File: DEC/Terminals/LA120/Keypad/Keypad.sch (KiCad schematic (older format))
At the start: 23 parts, among them J1 Conn_01x16, SW1 ENTER, SW10 9, SW11 0, SW12 COMMA, SW13 MINUS, SW14 PF1, SW15 PF2, SW16 PF3, SW17 PF4, SW18 PERIOD, SW2 1, SW3 2, SW4 3, SW5 4, SW6 5, SW7 6, SW8 7, SW9 8

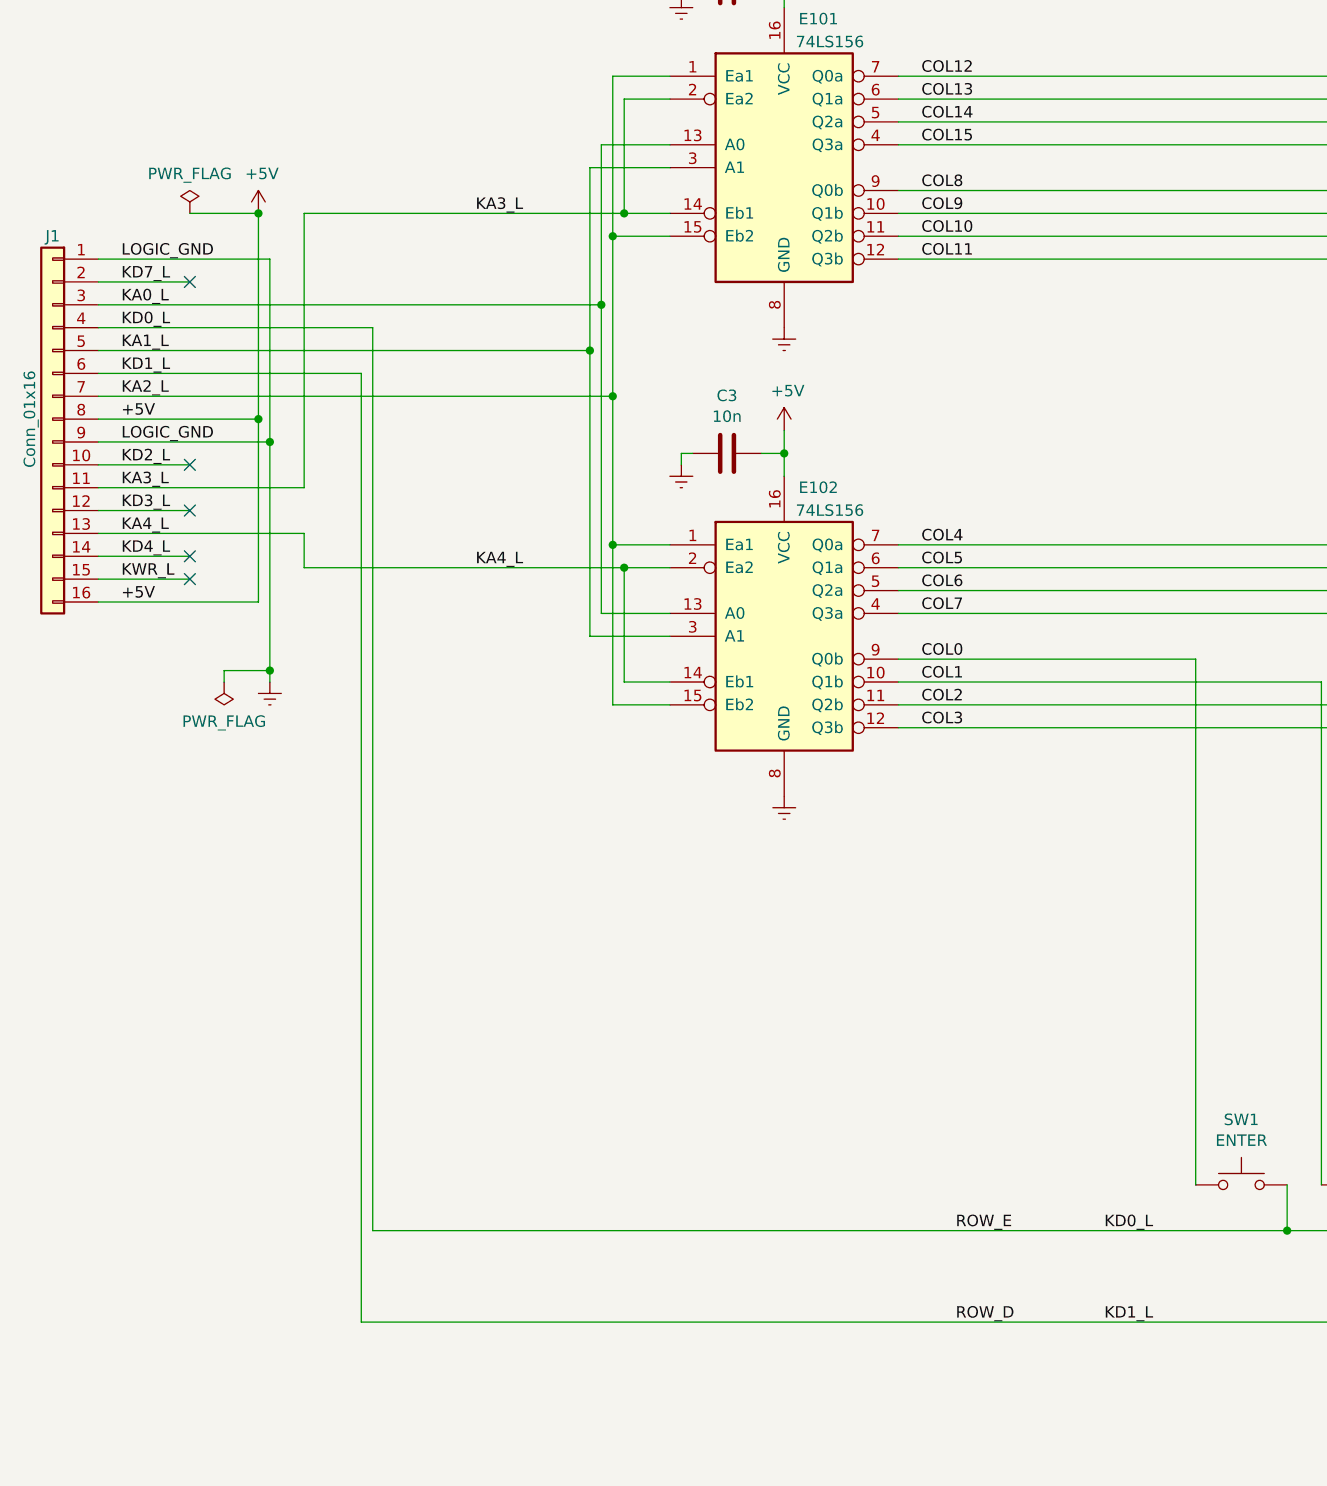
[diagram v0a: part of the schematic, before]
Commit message: Adds LA120 keyboard
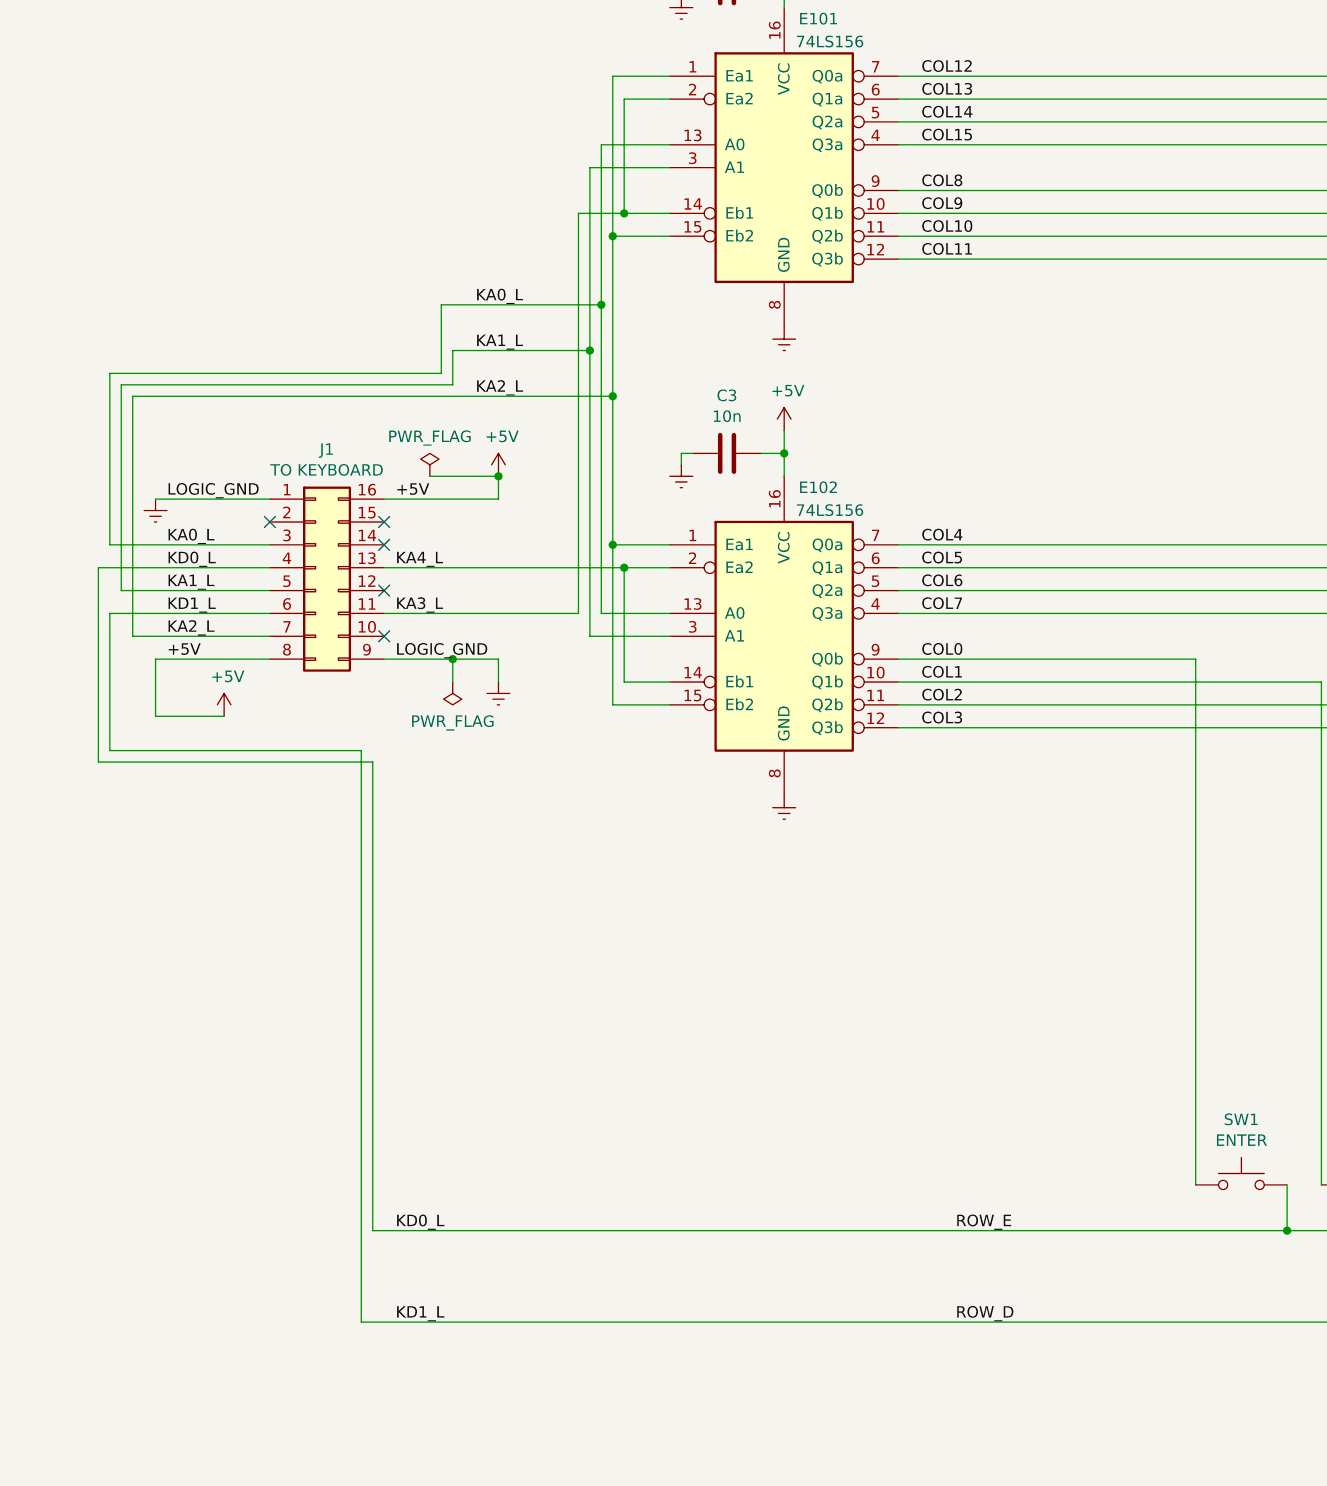
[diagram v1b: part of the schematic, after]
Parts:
- removed J1: Conn_01x16, symbol Connector_Generic:Conn_01x16
- added J1: TO KEYBOARD, symbol Connector_Generic:Conn_02x08_Counter_Clockwise
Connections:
- net +5V: now also J1.16 (Pin_16), J1.8 (Pin_8)
- net GNDREF: now also J1.1 (Pin_1), J1.9 (Pin_9)
- net KA0_L: now also J1.3 (Pin_3)
- net KA1_L: now also J1.5 (Pin_5)
- net KA2_L: now also J1.7 (Pin_7)
- net KA3_L: now also J1.11 (Pin_11)
- net KA4_L: now also J1.13 (Pin_13)
- net KD0_L: now also J1.4 (Pin_4)
- net KD1_L: now also J1.6 (Pin_6)
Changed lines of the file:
@@
 $EndDescr
-$Comp
-L Connector_Generic:Conn_01x16 J1
-U 1 1 5D1FAE3B
-P 1050 3750
-F 0 "J1" H 1050 4550 50  0000 C CNN
-F 1 "Conn_01x16" V 1150 3750 50  0000 C CNN
-F 2 "" H 1050 3750 50  0001 C CNN
-F 3 "~" H 1050 3750 50  0001 C CNN
-	1    1050 3750
-	-1   0    0    -1
-$EndComp
 $Comp
 L Switch:SW_Push SW1
@@
 	1    0    0    -1
 $EndComp
-Wire Wire Line
-	1250 3150 1650 3150
-Wire Wire Line
-	1250 3950 1650 3950
-Wire Wire Line
-	1250 4150 1650 4150
-Wire Wire Line
-	1250 4350 1650 4350
-Wire Wire Line
-	1250 4450 1650 4450
-Text Label 1350 3050 0    50   ~ 0
-LOGIC_GND
-Text Label 1350 3150 0    50   ~ 0
-KD7_L
-Text Label 1350 3750 0    50   ~ 0
-+5V
-Text Label 1350 4550 0    50   ~ 0
-+5V
-Text Label 1350 3850 0    50   ~ 0
-LOGIC_GND
-Text Label 1350 4050 0    50   ~ 0
-KA3_L
-Text Label 1350 4250 0    50   ~ 0
-KA4_L
-Text Label 1350 4450 0    50   ~ 0
-KWR_L
-Text Label 1350 3650 0    50   ~ 0
+Text Label 2900 3650 0    50   ~ 0
 KA2_L
-Text Label 1350 3450 0    50   ~ 0
+Text Label 2900 3450 0    50   ~ 0
 KA1_L
-Text Label 1350 3250 0    50   ~ 0
+Text Label 2900 3250 0    50   ~ 0
 KA0_L
-Text Label 1350 4350 0    50   ~ 0
-KD4_L
-Text Label 1350 4150 0    50   ~ 0
-KD3_L
-Text Label 1350 3950 0    50   ~ 0
-KD2_L
-Text Label 1350 3550 0    50   ~ 0
-KD1_L
-Text Label 1350 3350 0    50   ~ 0
-KD0_L
 $Comp
 L power:+5V #PWR0101
@@
 	3550 2850 3750 2850
 Wire Wire Line
-	3550 2850 2150 2850
-Wire Wire Line
-	2150 2850 2150 4050
-Wire Wire Line
-	1250 4050 2150 4050
+	3550 2850 3350 2850
 Connection ~ 3550 2850
-Text Label 2900 2850 0    50   ~ 0
-KA3_L
 Wire Wire Line
 	3750 2950 3500 2950
@@
 Wire Wire Line
 	3500 5000 3750 5000
-Wire Wire Line
-	3500 2950 3500 3650
 Connection ~ 3500 4300
 Wire Wire Line
@@
 Wire Wire Line
 	3550 4900 3750 4900
-Wire Wire Line
-	3550 4400 2150 4400
-Wire Wire Line
-	1250 4250 2150 4250
 Connection ~ 3550 4400
-Text Label 2900 4400 0    50   ~ 0
-KA4_L
 $Comp
 L Device:C C2
@@
 $EndComp
 Wire Wire Line
-	2150 4250 2150 4400
-Wire Wire Line
 	3750 2550 3450 2550
 Wire Wire Line
-	3450 2550 3450 3250
-Wire Wire Line
 	3450 4600 3750 4600
 Wire Wire Line
 	3750 4700 3400 4700
 Wire Wire Line
-	3400 4700 3400 3450
-Wire Wire Line
 	3400 2650 3750 2650
-Wire Wire Line
-	1250 3250 3450 3250
-Connection ~ 3450 3250
-Wire Wire Line
-	3450 3250 3450 4600
-Wire Wire Line
-	1250 3450 3400 3450
-Connection ~ 3400 3450
-Wire Wire Line
-	3400 3450 3400 2650
-Connection ~ 3500 3650
-Wire Wire Line
-	3500 3650 3500 4300
-Wire Wire Line
-	1250 3650 3500 3650
-Wire Wire Line
-	2000 3850 2000 4850
-Wire Wire Line
-	1250 3850 2000 3850
-Wire Wire Line
-	2000 3050 2000 3850
-Wire Wire Line
-	1250 3050 2000 3050
-Connection ~ 2000 3850
 $Comp
 L power:GNDREF #PWR0107
 U 1 1 5D22E3D0
-P 2000 4900
-F 0 "#PWR0107" H 2000 4650 50  0001 C CNN
-F 1 "GNDREF" H 2005 4727 50  0001 C CNN
-F 2 "" H 2000 4900 50  0001 C CNN
-F 3 "" H 2000 4900 50  0001 C CNN
-	1    2000 4900
-	1    0    0    -1
-$EndComp
-Wire Wire Line
-	1950 3750 1950 2850
-Wire Wire Line
-	1250 3750 1950 3750
+P 3000 4900
+F 0 "#PWR0107" H 3000 4650 50  0001 C CNN
+F 1 "GNDREF" H 3005 4727 50  0001 C CNN
+F 2 "" H 3000 4900 50  0001 C CNN
+F 3 "" H 3000 4900 50  0001 C CNN
+	1    3000 4900
+	1    0    0    -1
+$EndComp
 $Comp
 L power:+5V #PWR0108
 U 1 1 5D22FB53
-P 1950 2850
-F 0 "#PWR0108" H 1950 2700 50  0001 C CNN
-F 1 "+5V" H 1965 3023 50  0000 C CNN
-F 2 "" H 1950 2850 50  0001 C CNN
-F 3 "" H 1950 2850 50  0001 C CNN
-	1    1950 2850
-	1    0    0    -1
-$EndComp
-Wire Wire Line
-	1950 4550 1950 3750
-Wire Wire Line
-	1250 4550 1950 4550
-Connection ~ 1950 3750
-NoConn ~ 1650 3150
-NoConn ~ 1650 4150
-NoConn ~ 1650 3950
-NoConn ~ 1650 4350
-NoConn ~ 1650 4450
+P 3000 4000
+F 0 "#PWR0108" H 3000 3850 50  0001 C CNN
+F 1 "+5V" H 3015 4173 50  0000 C CNN
+F 2 "" H 3000 4000 50  0001 C CNN
+F 3 "" H 3000 4000 50  0001 C CNN
+	1    3000 4000
+	1    0    0    -1
+$EndComp
 Wire Wire Line
 	6450 7100 6450 7300
@@
 	6450 7300 2450 7300
 Wire Wire Line
-	2450 7300 2450 3350
-Wire Wire Line
-	1250 3350 2450 3350
+	2450 7300 2450 5250
 Connection ~ 6450 7300
-Text Label 5650 7300 0    50   ~ 0
+Text Label 2550 7300 0    50   ~ 0
 KD0_L
 Wire Wire Line
-	2400 3550 2400 7700
-Wire Wire Line
 	2400 7700 12550 7700
 Wire Wire Line
@@
 Wire Wire Line
 	12550 6600 12500 6600
-Wire Wire Line
-	1250 3550 2400 3550
 Wire Wire Line
 	12550 7700 14750 7700
@@
 	14750 6600 14700 6600
 Connection ~ 12550 7700
-Text Label 5650 7700 0    50   ~ 0
+Text Label 2550 7700 0    50   ~ 0
 KD1_L
 Wire Wire Line
@@
 L power:PWR_FLAG #FLG0101
 U 1 1 5D294754
-P 1800 4900
-F 0 "#FLG0101" H 1800 4975 50  0001 C CNN
-F 1 "PWR_FLAG" H 1800 5073 50  0000 C CNN
-F 2 "" H 1800 4900 50  0001 C CNN
-F 3 "~" H 1800 4900 50  0001 C CNN
-	1    1800 4900
+P 2800 4900
+F 0 "#FLG0101" H 2800 4975 50  0001 C CNN
+F 1 "PWR_FLAG" H 2800 5073 50  0000 C CNN
+F 2 "" H 2800 4900 50  0001 C CNN
+F 3 "~" H 2800 4900 50  0001 C CNN
+	1    2800 4900
 	-1   0    0    1
 $EndComp
-Wire Wire Line
-	1800 4900 1800 4850
-Wire Wire Line
-	1800 4850 2000 4850
-Connection ~ 2000 4850
-Wire Wire Line
-	2000 4850 2000 4900
 $Comp
 L power:PWR_FLAG #FLG0102
 U 1 1 5D299778
-P 1650 2850
-F 0 "#FLG0102" H 1650 2925 50  0001 C CNN
-F 1 "PWR_FLAG" H 1650 3023 50  0000 C CNN
-F 2 "" H 1650 2850 50  0001 C CNN
-F 3 "~" H 1650 2850 50  0001 C CNN
-	1    1650 2850
-	1    0    0    -1
-$EndComp
-Wire Wire Line
-	1650 2850 1950 2850
-Connection ~ 1950 2850
+P 2700 4000
+F 0 "#FLG0102" H 2700 4075 50  0001 C CNN
+F 1 "PWR_FLAG" H 2700 4173 50  0000 C CNN
+F 2 "" H 2700 4000 50  0001 C CNN
+F 3 "~" H 2700 4000 50  0001 C CNN
+	1    2700 4000
+	1    0    0    -1
+$EndComp
+Wire Wire Line
+	2700 4000 3000 4000
 Text Notes 11900 10250 0    70   ~ 0
 SCHEMATIC REFORMATTED FROM "LA120 FIELD MAINTENANCE PRINT SET",\nDIGITAL EQUIPMENT CORPORATION, SEP 1978.
@@
 Text Notes 15450 11050 0    50   ~ 0
 A
+$Comp
+L Connector_Generic:Conn_02x08_Counter_Clockwise J1
+U 1 1 5D2612E0
+P 2200 4400
+F 0 "J1" H 2250 4917 50  0000 C CNN
+F 1 "TO KEYBOARD" H 2250 4826 50  0000 C CNN
+F 2 "" H 2200 4400 50  0001 C CNN
+F 3 "~" H 2200 4400 50  0001 C CNN
+	1    2200 4400
+	1    0    0    -1
+$EndComp
+Wire Wire Line
+	2000 4100 1500 4100
+Text Label 1550 4100 0    50   ~ 0
+LOGIC_GND
+NoConn ~ 2000 4200
+Text Label 1550 4800 0    50   ~ 0
++5V
+Wire Wire Line
+	2000 4800 1500 4800
+Text Label 1550 4300 0    50   ~ 0
+KA0_L
+Text Label 1550 4400 0    50   ~ 0
+KD0_L
+Text Label 1550 4500 0    50   ~ 0
+KA1_L
+Text Label 1550 4600 0    50   ~ 0
+KD1_L
+Text Label 1550 4700 0    50   ~ 0
+KA2_L
+Wire Wire Line
+	2500 4800 2800 4800
+Text Label 2550 4800 0    50   ~ 0
+LOGIC_GND
+Text Label 2550 4600 0    50   ~ 0
+KA3_L
+Text Label 2550 4400 0    50   ~ 0
+KA4_L
+Text Label 2550 4100 0    50   ~ 0
++5V
+NoConn ~ 2500 4200
+NoConn ~ 2500 4300
+NoConn ~ 2500 4500
+NoConn ~ 2500 4700
+Wire Wire Line
+	3500 3650 3500 4300
+Wire Wire Line
+	3500 2950 3500 3650
+Connection ~ 3500 3650
+Wire Wire Line
+	3400 3450 3400 2650
+Wire Wire Line
+	3400 4700 3400 3450
+Connection ~ 3400 3450
+Wire Wire Line
+	3450 3250 3450 4600
+Wire Wire Line
+	3450 2550 3450 3250
+Connection ~ 3450 3250
+Wire Wire Line
+	3000 4800 3000 4900
+Wire Wire Line
+	2800 4800 2800 4900
+Connection ~ 2800 4800
+Wire Wire Line
+	2800 4800 3000 4800
+$Comp
+L power:GNDREF #PWR?
+U 1 1 5D2F3923
+P 1500 4100
+F 0 "#PWR?" H 1500 3850 50  0001 C CNN
+F 1 "GNDREF" H 1505 3927 50  0001 C CNN
+F 2 "" H 1500 4100 50  0001 C CNN
+F 3 "" H 1500 4100 50  0001 C CNN
+	1    1500 4100
+	1    0    0    -1
+$EndComp
+Wire Wire Line
+	3000 4100 3000 4000
+Wire Wire Line
+	2500 4100 3000 4100
+Connection ~ 3000 4000
+$Comp
+L power:+5V #PWR?
+U 1 1 5D304DAF
+P 1800 5050
+F 0 "#PWR?" H 1800 4900 50  0001 C CNN
+F 1 "+5V" H 1815 5223 50  0000 C CNN
+F 2 "" H 1800 5050 50  0001 C CNN
+F 3 "" H 1800 5050 50  0001 C CNN
+	1    1800 5050
+	1    0    0    -1
+$EndComp
+Wire Wire Line
+	1500 4800 1500 5050
+Wire Wire Line
+	1500 5050 1800 5050
+Wire Wire Line
+	2500 4400 3550 4400
+Wire Wire Line
+	3350 4600 3350 2850
+Wire Wire Line
+	2500 4600 3350 4600
+Wire Wire Line
+	1400 4700 1400 3650
+Wire Wire Line
+	1400 4700 2000 4700
+Wire Wire Line
+	1400 3650 3500 3650
+Wire Wire Line
+	1350 4500 1350 3600
+Wire Wire Line
+	1350 3600 2800 3600
+Wire Wire Line
+	2800 3600 2800 3450
+Wire Wire Line
+	1350 4500 2000 4500
+Wire Wire Line
+	2800 3450 3400 3450
+Wire Wire Line
+	1300 4300 1300 3550
+Wire Wire Line
+	1300 3550 2750 3550
+Wire Wire Line
+	2750 3550 2750 3250
+Wire Wire Line
+	1300 4300 2000 4300
+Wire Wire Line
+	2750 3250 3450 3250
+Wire Wire Line
+	1300 4600 1300 5200
+Wire Wire Line
+	1300 5200 2400 5200
+Wire Wire Line
+	1300 4600 2000 4600
+Wire Wire Line
+	2400 5200 2400 7700
+Wire Wire Line
+	1250 4400 1250 5250
+Wire Wire Line
+	1250 5250 2450 5250
+Wire Wire Line
+	1250 4400 2000 4400
 $EndSCHEMATC
